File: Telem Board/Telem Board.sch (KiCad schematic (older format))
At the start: 21 parts, among them J1 MAIN, J2 NTC1, J3 NTC2, J4 NTC3, J5 NTC4, J6 6S, U1 LM1117-3.3, U2 MCP3208

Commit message: finish sch
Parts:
- added C8, C9: 1uF, Capacitor_SMD:C_0805_2012Metric_Pad1.18x1.45mm_HandSolder, symbol Device:C
- added H1, H2, H3, H4: MountingHole, MountingHole:MountingHole_3.2mm_M3, symbol Mechanical:MountingHole
- C1, C2, C3, C4, C6, C7: footprint (none) -> Capacitor_SMD:C_0805_2012Metric_Pad1.18x1.45mm_HandSolder
- C5: value 1uF -> 0.47uF; footprint (none) -> Capacitor_SMD:C_0805_2012Metric_Pad1.18x1.45mm_HandSolder
- J1: footprint (none) -> Connector_PinHeader_2.54mm:PinHeader_1x07_P2.54mm_Vertical
- J2, J3, J4, J5: footprint (none) -> Connector_PinHeader_2.54mm:PinHeader_1x02_P2.54mm_Vertical
- J6: footprint (none) -> Connector_AMASS:AMASS_XT60-M_1x02_P7.20mm_Vertical
- R1, R2, R3, R4, R5, R6: footprint (none) -> Capacitor_SMD:C_1206_3216Metric_Pad1.33x1.80mm_HandSolder
- U1: footprint (none) -> Package_TO_SOT_SMD:SOT-223-3_TabPin2
- U2: footprint (none) -> Package_DIP:DIP-16_W7.62mm
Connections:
- net +3V3: now also C8.1, C9.1
- net GNDA: now also C8.2, C9.2
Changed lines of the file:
@@
 F 0 "U2" H 5000 3650 50  0000 C CNN
 F 1 "MCP3208" H 5000 3550 50  0000 C CNN
-F 2 "" H 5450 3150 50  0001 C CNN
+F 2 "Package_DIP:DIP-16_W7.62mm" H 5450 3150 50  0001 C CNN
 F 3 "http://ww1.microchip.com/downloads/en/DeviceDoc/21298c.pdf" H 5450 3150 50  0001 C CNN
 	1    5350 3050
@@
 F 0 "J1" H 7722 3024 50  0000 R CNN
 F 1 "MAIN" H 7722 2933 50  0000 R CNN
-F 2 "" H 7750 3000 50  0001 C CNN
+F 2 "Connector_PinHeader_2.54mm:PinHeader_1x07_P2.54mm_Vertical" H 7750 3000 50  0001 C CNN
 F 3 "~" H 7750 3000 50  0001 C CNN
 	1    7750 3000
@@
 F 0 "U1" H 6750 2342 50  0000 C CNN
 F 1 "LM1117-3.3" H 6750 2251 50  0000 C CNN
-F 2 "" H 6750 2100 50  0001 C CNN
+F 2 "Package_TO_SOT_SMD:SOT-223-3_TabPin2" H 6750 2100 50  0001 C CNN
 F 3 "http://www.ti.com/lit/ds/symlink/lm1117.pdf" H 6750 2100 50  0001 C CNN
 	1    6750 2100
@@
 F 0 "C7" H 7265 2296 50  0000 L CNN
 F 1 "10uF" H 7265 2205 50  0000 L CNN
-F 2 "" H 7188 2100 50  0001 C CNN
+F 2 "Capacitor_SMD:C_0805_2012Metric_Pad1.18x1.45mm_HandSolder" H 7188 2100 50  0001 C CNN
 F 3 "~" H 7150 2250 50  0001 C CNN
 	1    7150 2250
@@
 F 0 "C6" H 6315 2296 50  0000 L CNN
 F 1 "10uF" H 6315 2205 50  0000 L CNN
-F 2 "" H 6238 2100 50  0001 C CNN
+F 2 "Capacitor_SMD:C_0805_2012Metric_Pad1.18x1.45mm_HandSolder" H 6238 2100 50  0001 C CNN
 F 3 "~" H 6200 2250 50  0001 C CNN
 	1    6200 2250
@@
 F 0 "R1" H 3350 2350 50  0000 L CNN
 F 1 "33K" V 3300 2250 50  0000 L CNN
-F 2 "" V 3230 2350 50  0001 C CNN
+F 2 "Capacitor_SMD:C_1206_3216Metric_Pad1.33x1.80mm_HandSolder" V 3230 2350 50  0001 C CNN
 F 3 "~" H 3300 2350 50  0001 C CNN
 	1    3300 2350
@@
 P 3650 1150
 F 0 "R5" H 3720 1196 50  0000 L CNN
-F 1 "250K" H 3720 1105 50  0000 L CNN
-F 2 "" V 3580 1150 50  0001 C CNN
+F 1 "250K" V 3650 1050 50  0000 L CNN
+F 2 "Capacitor_SMD:C_1206_3216Metric_Pad1.33x1.80mm_HandSolder" V 3580 1150 50  0001 C CNN
 F 3 "~" H 3650 1150 50  0001 C CNN
 	1    3650 1150
@@
 P 3650 1550
 F 0 "R6" H 3720 1596 50  0000 L CNN
-F 1 "27K" H 3720 1505 50  0000 L CNN
-F 2 "" V 3580 1550 50  0001 C CNN
+F 1 "27K" V 3650 1450 50  0000 L CNN
+F 2 "Capacitor_SMD:C_1206_3216Metric_Pad1.33x1.80mm_HandSolder" V 3580 1550 50  0001 C CNN
 F 3 "~" H 3650 1550 50  0001 C CNN
 	1    3650 1550
@@
 F 0 "J6" H 2858 1181 50  0000 C CNN
 F 1 "6S" H 2858 1090 50  0000 C CNN
-F 2 "" H 2750 1000 50  0001 C CNN
+F 2 "Connector_AMASS:AMASS_XT60-M_1x02_P7.20mm_Vertical" H 2750 1000 50  0001 C CNN
 F 3 "~" H 2750 1000 50  0001 C CNN
 	1    2750 1000
@@
 P 4050 1500
 F 0 "C5" H 4165 1546 50  0000 L CNN
-F 1 "1uF" H 4165 1455 50  0000 L CNN
-F 2 "" H 4088 1350 50  0001 C CNN
+F 1 "0.47uF" H 4165 1455 50  0000 L CNN
+F 2 "Capacitor_SMD:C_0805_2012Metric_Pad1.18x1.45mm_HandSolder" H 4088 1350 50  0001 C CNN
 F 3 "~" H 4050 1500 50  0001 C CNN
 	1    4050 1500
@@
 F 0 "J2" H 2858 2681 50  0000 C CNN
 F 1 "NTC1" H 2858 2590 50  0000 C CNN
-F 2 "" H 2750 2500 50  0001 C CNN
+F 2 "Connector_PinHeader_2.54mm:PinHeader_1x02_P2.54mm_Vertical" H 2750 2500 50  0001 C CNN
 F 3 "~" H 2750 2500 50  0001 C CNN
 	1    2750 2500
@@
 F 0 "C1" H 3415 2696 50  0000 L CNN
 F 1 "0.1uF" H 3415 2605 50  0000 L CNN
-F 2 "" H 3338 2500 50  0001 C CNN
+F 2 "Capacitor_SMD:C_0805_2012Metric_Pad1.18x1.45mm_HandSolder" H 3338 2500 50  0001 C CNN
 F 3 "~" H 3300 2650 50  0001 C CNN
 	1    3300 2650
@@
 F 0 "R2" H 3350 3000 50  0000 L CNN
 F 1 "33K" V 3300 2900 50  0000 L CNN
-F 2 "" V 3230 3000 50  0001 C CNN
+F 2 "Capacitor_SMD:C_1206_3216Metric_Pad1.33x1.80mm_HandSolder" V 3230 3000 50  0001 C CNN
 F 3 "~" H 3300 3000 50  0001 C CNN
 	1    3300 3000
@@
 F 0 "R3" H 3350 3650 50  0000 L CNN
 F 1 "33K" V 3300 3550 50  0000 L CNN
-F 2 "" V 3230 3650 50  0001 C CNN
+F 2 "Capacitor_SMD:C_1206_3216Metric_Pad1.33x1.80mm_HandSolder" V 3230 3650 50  0001 C CNN
 F 3 "~" H 3300 3650 50  0001 C CNN
 	1    3300 3650
@@
 F 0 "R4" H 3350 4300 50  0000 L CNN
 F 1 "33K" V 3300 4200 50  0000 L CNN
-F 2 "" V 3230 4300 50  0001 C CNN
+F 2 "Capacitor_SMD:C_1206_3216Metric_Pad1.33x1.80mm_HandSolder" V 3230 4300 50  0001 C CNN
 F 3 "~" H 3300 4300 50  0001 C CNN
 	1    3300 4300
@@
 F 0 "C2" H 3415 3346 50  0000 L CNN
 F 1 "0.1uF" H 3415 3255 50  0000 L CNN
-F 2 "" H 3338 3150 50  0001 C CNN
+F 2 "Capacitor_SMD:C_0805_2012Metric_Pad1.18x1.45mm_HandSolder" H 3338 3150 50  0001 C CNN
 F 3 "~" H 3300 3300 50  0001 C CNN
 	1    3300 3300
@@
 F 0 "J5" H 2858 4631 50  0000 C CNN
 F 1 "NTC4" H 2858 4540 50  0000 C CNN
-F 2 "" H 2750 4450 50  0001 C CNN
+F 2 "Connector_PinHeader_2.54mm:PinHeader_1x02_P2.54mm_Vertical" H 2750 4450 50  0001 C CNN
 F 3 "~" H 2750 4450 50  0001 C CNN
 	1    2750 4450
@@
 F 0 "J4" H 2858 3981 50  0000 C CNN
 F 1 "NTC3" H 2858 3890 50  0000 C CNN
-F 2 "" H 2750 3800 50  0001 C CNN
+F 2 "Connector_PinHeader_2.54mm:PinHeader_1x02_P2.54mm_Vertical" H 2750 3800 50  0001 C CNN
 F 3 "~" H 2750 3800 50  0001 C CNN
 	1    2750 3800
@@
 F 0 "J3" H 2858 3331 50  0000 C CNN
 F 1 "NTC2" H 2858 3240 50  0000 C CNN
-F 2 "" H 2750 3150 50  0001 C CNN
+F 2 "Connector_PinHeader_2.54mm:PinHeader_1x02_P2.54mm_Vertical" H 2750 3150 50  0001 C CNN
 F 3 "~" H 2750 3150 50  0001 C CNN
 	1    2750 3150
@@
 F 0 "C3" H 3415 3996 50  0000 L CNN
 F 1 "0.1uF" H 3415 3905 50  0000 L CNN
-F 2 "" H 3338 3800 50  0001 C CNN
+F 2 "Capacitor_SMD:C_0805_2012Metric_Pad1.18x1.45mm_HandSolder" H 3338 3800 50  0001 C CNN
 F 3 "~" H 3300 3950 50  0001 C CNN
 	1    3300 3950
@@
 F 0 "C4" H 3415 4646 50  0000 L CNN
 F 1 "0.1uF" H 3415 4555 50  0000 L CNN
-F 2 "" H 3338 4450 50  0001 C CNN
+F 2 "Capacitor_SMD:C_0805_2012Metric_Pad1.18x1.45mm_HandSolder" H 3338 4450 50  0001 C CNN
 F 3 "~" H 3300 4600 50  0001 C CNN
 	1    3300 4600
@@
 Text Notes 2300 650  0    50   ~ 0
 Input capacitors used to reduce effective input impedance
+$Comp
+L Mechanical:MountingHole H1
+U 1 1 61908367
+P 8600 750
+F 0 "H1" H 8700 796 50  0000 L CNN
+F 1 "MountingHole" H 8700 705 50  0000 L CNN
+F 2 "MountingHole:MountingHole_3.2mm_M3" H 8600 750 50  0001 C CNN
+F 3 "~" H 8600 750 50  0001 C CNN
+	1    8600 750
+	1    0    0    -1
+$EndComp
+$Comp
+L Mechanical:MountingHole H2
+U 1 1 61908C54
+P 9350 750
+F 0 "H2" H 9450 796 50  0000 L CNN
+F 1 "MountingHole" H 9450 705 50  0000 L CNN
+F 2 "MountingHole:MountingHole_3.2mm_M3" H 9350 750 50  0001 C CNN
+F 3 "~" H 9350 750 50  0001 C CNN
+	1    9350 750
+	1    0    0    -1
+$EndComp
+$Comp
+L Mechanical:MountingHole H3
+U 1 1 61909B9E
+P 8600 1000
+F 0 "H3" H 8700 1046 50  0000 L CNN
+F 1 "MountingHole" H 8700 955 50  0000 L CNN
+F 2 "MountingHole:MountingHole_3.2mm_M3" H 8600 1000 50  0001 C CNN
+F 3 "~" H 8600 1000 50  0001 C CNN
+	1    8600 1000
+	1    0    0    -1
+$EndComp
+$Comp
+L Mechanical:MountingHole H4
+U 1 1 6190AC4C
+P 9350 1000
+F 0 "H4" H 9450 1046 50  0000 L CNN
+F 1 "MountingHole" H 9450 955 50  0000 L CNN
+F 2 "MountingHole:MountingHole_3.2mm_M3" H 9350 1000 50  0001 C CNN
+F 3 "~" H 9350 1000 50  0001 C CNN
+	1    9350 1000
+	1    0    0    -1
+$EndComp
+$Comp
+L Device:C C9
+U 1 1 61914F1A
+P 6350 2700
+F 0 "C9" H 6465 2746 50  0000 L CNN
+F 1 "1uF" H 6465 2655 50  0000 L CNN
+F 2 "Capacitor_SMD:C_0805_2012Metric_Pad1.18x1.45mm_HandSolder" H 6388 2550 50  0001 C CNN
+F 3 "~" H 6350 2700 50  0001 C CNN
+	1    6350 2700
+	1    0    0    -1
+$EndComp
+$Comp
+L Device:C C8
+U 1 1 61915AD3
+P 4250 2700
+F 0 "C8" H 4365 2746 50  0000 L CNN
+F 1 "1uF" H 4365 2655 50  0000 L CNN
+F 2 "Capacitor_SMD:C_0805_2012Metric_Pad1.18x1.45mm_HandSolder" H 4288 2550 50  0001 C CNN
+F 3 "~" H 4250 2700 50  0001 C CNN
+	1    4250 2700
+	1    0    0    -1
+$EndComp
+Wire Wire Line
+	5250 2550 4250 2550
+Connection ~ 5250 2550
+Wire Wire Line
+	4250 2850 4250 3650
+Wire Wire Line
+	4250 3650 5250 3650
+Wire Wire Line
+	5550 2550 6350 2550
+Wire Wire Line
+	6350 2850 6350 3650
+Wire Wire Line
+	6350 3650 5550 3650
 $EndSCHEMATC

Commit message: route
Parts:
- removed C9: 1uF, Capacitor_SMD:C_0805_2012Metric_Pad1.18x1.45mm_HandSolder, symbol Device:C
- removed H3, H4: MountingHole, MountingHole:MountingHole_3.2mm_M3, symbol Mechanical:MountingHole
- H1, H2: footprint MountingHole:MountingHole_3.2mm_M3 -> MountingHole:MountingHole_2.7mm_M2.5
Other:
- moved on the sheet: C8
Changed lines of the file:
@@
 	1    0    0    -1
 $EndComp
-Wire Wire Line
-	5550 2550 5250 2550
 Connection ~ 5550 2550
 $Comp
@@
 	1    0    0    -1
 $EndComp
-Wire Wire Line
-	5550 3650 5250 3650
 Connection ~ 5550 3650
 Connection ~ 5250 3650
@@
 F 0 "H1" H 8700 796 50  0000 L CNN
 F 1 "MountingHole" H 8700 705 50  0000 L CNN
-F 2 "MountingHole:MountingHole_3.2mm_M3" H 8600 750 50  0001 C CNN
+F 2 "MountingHole:MountingHole_2.7mm_M2.5" H 8600 750 50  0001 C CNN
 F 3 "~" H 8600 750 50  0001 C CNN
 	1    8600 750
@@
 F 0 "H2" H 9450 796 50  0000 L CNN
 F 1 "MountingHole" H 9450 705 50  0000 L CNN
-F 2 "MountingHole:MountingHole_3.2mm_M3" H 9350 750 50  0001 C CNN
+F 2 "MountingHole:MountingHole_2.7mm_M2.5" H 9350 750 50  0001 C CNN
 F 3 "~" H 9350 750 50  0001 C CNN
 	1    9350 750
@@
 $EndComp
 $Comp
-L Mechanical:MountingHole H3
-U 1 1 61909B9E
-P 8600 1000
-F 0 "H3" H 8700 1046 50  0000 L CNN
-F 1 "MountingHole" H 8700 955 50  0000 L CNN
-F 2 "MountingHole:MountingHole_3.2mm_M3" H 8600 1000 50  0001 C CNN
-F 3 "~" H 8600 1000 50  0001 C CNN
-	1    8600 1000
-	1    0    0    -1
-$EndComp
-$Comp
-L Mechanical:MountingHole H4
-U 1 1 6190AC4C
-P 9350 1000
-F 0 "H4" H 9450 1046 50  0000 L CNN
-F 1 "MountingHole" H 9450 955 50  0000 L CNN
-F 2 "MountingHole:MountingHole_3.2mm_M3" H 9350 1000 50  0001 C CNN
-F 3 "~" H 9350 1000 50  0001 C CNN
-	1    9350 1000
-	1    0    0    -1
-$EndComp
-$Comp
-L Device:C C9
-U 1 1 61914F1A
+L Device:C C8
+U 1 1 61915AD3
 P 6350 2700
-F 0 "C9" H 6465 2746 50  0000 L CNN
+F 0 "C8" H 6465 2746 50  0000 L CNN
 F 1 "1uF" H 6465 2655 50  0000 L CNN
 F 2 "Capacitor_SMD:C_0805_2012Metric_Pad1.18x1.45mm_HandSolder" H 6388 2550 50  0001 C CNN
@@
 	1    0    0    -1
 $EndComp
-$Comp
-L Device:C C8
-U 1 1 61915AD3
-P 4250 2700
-F 0 "C8" H 4365 2746 50  0000 L CNN
-F 1 "1uF" H 4365 2655 50  0000 L CNN
-F 2 "Capacitor_SMD:C_0805_2012Metric_Pad1.18x1.45mm_HandSolder" H 4288 2550 50  0001 C CNN
-F 3 "~" H 4250 2700 50  0001 C CNN
-	1    4250 2700
-	1    0    0    -1
-$EndComp
-Wire Wire Line
-	5250 2550 4250 2550
-Connection ~ 5250 2550
-Wire Wire Line
-	4250 2850 4250 3650
-Wire Wire Line
-	4250 3650 5250 3650
-Wire Wire Line
-	5550 2550 6350 2550
+Wire Wire Line
+	6350 2550 5550 2550
 Wire Wire Line
 	6350 2850 6350 3650
 Wire Wire Line
-	6350 3650 5550 3650
+	5250 2550 5550 2550
+Wire Wire Line
+	5550 3650 6350 3650
+Wire Wire Line
+	5250 3650 5550 3650
 $EndSCHEMATC

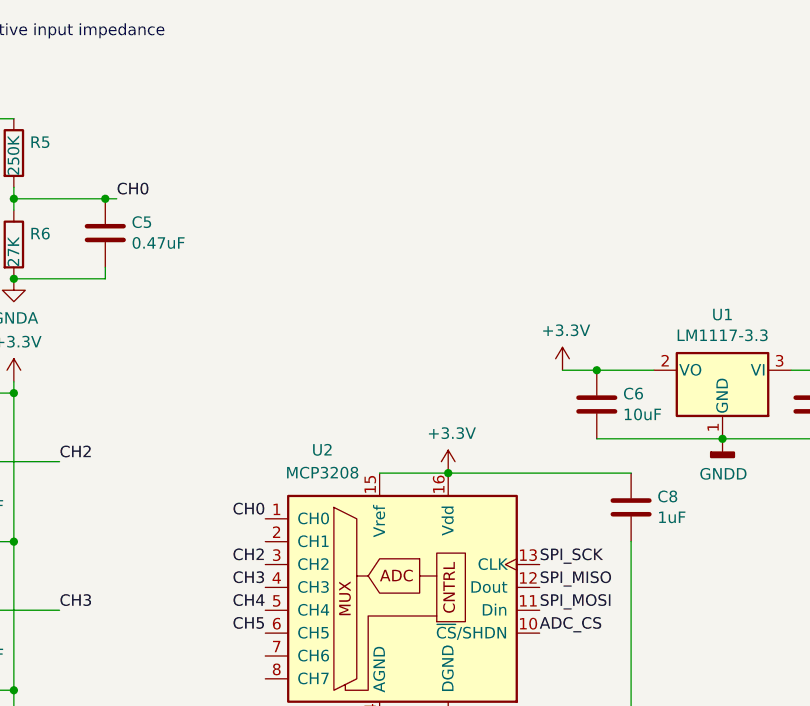
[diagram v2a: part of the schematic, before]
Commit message: add 3s battery in
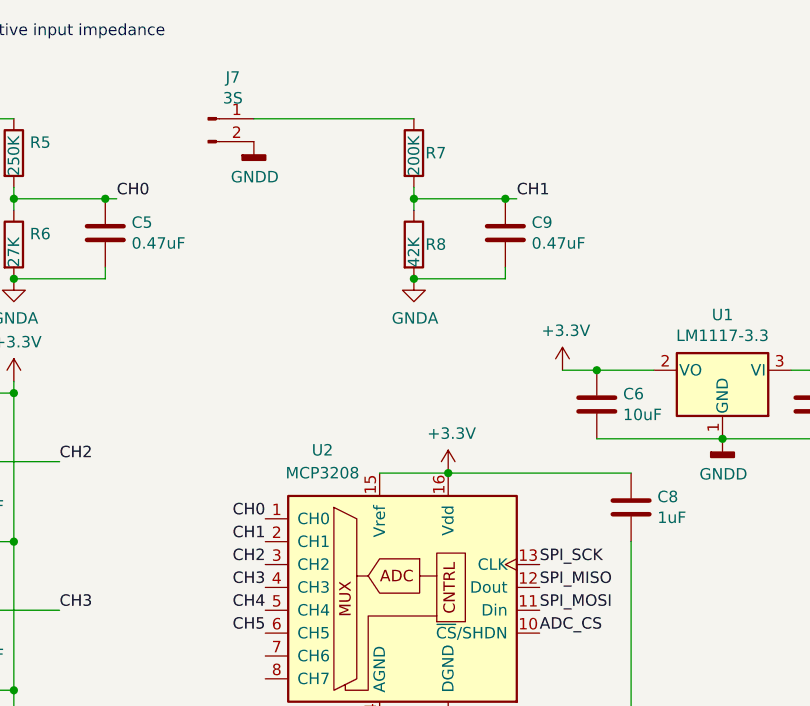
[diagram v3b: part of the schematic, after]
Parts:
- added C9: 0.47uF, Capacitor_SMD:C_0805_2012Metric_Pad1.18x1.45mm_HandSolder, symbol Device:C
- added J7: 3S, Connector_AMASS:AMASS_XT60-M_1x02_P7.20mm_Vertical, symbol Connector:Conn_01x02_Male
- added R7: 200K, Capacitor_SMD:C_1206_3216Metric_Pad1.33x1.80mm_HandSolder, symbol Device:R
- added R8: 42K, Capacitor_SMD:C_1206_3216Metric_Pad1.33x1.80mm_HandSolder, symbol Device:R
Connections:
- net GNDA: now also C9.2, J7.2 (Pin_2), R8.2
- net CH1: now reaches U2.2 (CH1)
- net CH1: now also C9.1, R7.2, R8.1
- new net: J7.1 (Pin_1), R7.1
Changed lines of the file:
@@
 Wire Wire Line
 	5250 3650 5550 3650
+$Comp
+L Device:R R7
+U 1 1 6191565F
+P 5400 1150
+F 0 "R7" H 5450 1150 50  0000 L CNN
+F 1 "200K" V 5400 1050 50  0000 L CNN
+F 2 "Capacitor_SMD:C_1206_3216Metric_Pad1.33x1.80mm_HandSolder" V 5330 1150 50  0001 C CNN
+F 3 "~" H 5400 1150 50  0001 C CNN
+	1    5400 1150
+	1    0    0    -1
+$EndComp
+$Comp
+L Device:R R8
+U 1 1 61915665
+P 5400 1550
+F 0 "R8" H 5450 1550 50  0000 L CNN
+F 1 "42K" V 5400 1450 50  0000 L CNN
+F 2 "Capacitor_SMD:C_1206_3216Metric_Pad1.33x1.80mm_HandSolder" V 5330 1550 50  0001 C CNN
+F 3 "~" H 5400 1550 50  0001 C CNN
+	1    5400 1550
+	1    0    0    -1
+$EndComp
+$Comp
+L power:GNDA #PWR014
+U 1 1 6191566B
+P 5400 1700
+F 0 "#PWR014" H 5400 1450 50  0001 C CNN
+F 1 "GNDA" H 5405 1527 50  0000 C CNN
+F 2 "" H 5400 1700 50  0001 C CNN
+F 3 "" H 5400 1700 50  0001 C CNN
+	1    5400 1700
+	1    0    0    -1
+$EndComp
+Wire Wire Line
+	5400 1300 5400 1350
+Connection ~ 5400 1350
+Wire Wire Line
+	5400 1350 5400 1400
+Text Label 5850 1350 0    50   ~ 0
+CH1
+$Comp
+L Connector:Conn_01x02_Male J7
+U 1 1 61915675
+P 4500 1000
+F 0 "J7" H 4608 1181 50  0000 C CNN
+F 1 "3S" H 4608 1090 50  0000 C CNN
+F 2 "Connector_AMASS:AMASS_XT60-M_1x02_P7.20mm_Vertical" H 4500 1000 50  0001 C CNN
+F 3 "~" H 4500 1000 50  0001 C CNN
+	1    4500 1000
+	1    0    0    -1
+$EndComp
+Wire Wire Line
+	4700 1000 5400 1000
+$Comp
+L power:GNDD #PWR013
+U 1 1 6191567C
+P 4700 1100
+F 0 "#PWR013" H 4700 850 50  0001 C CNN
+F 1 "GNDD" H 4704 945 50  0000 C CNN
+F 2 "" H 4700 1100 50  0001 C CNN
+F 3 "" H 4700 1100 50  0001 C CNN
+	1    4700 1100
+	1    0    0    -1
+$EndComp
+Wire Wire Line
+	5400 1350 5800 1350
+$Comp
+L Device:C C9
+U 1 1 61915683
+P 5800 1500
+F 0 "C9" H 5915 1546 50  0000 L CNN
+F 1 "0.47uF" H 5915 1455 50  0000 L CNN
+F 2 "Capacitor_SMD:C_0805_2012Metric_Pad1.18x1.45mm_HandSolder" H 5838 1350 50  0001 C CNN
+F 3 "~" H 5800 1500 50  0001 C CNN
+	1    5800 1500
+	1    0    0    -1
+$EndComp
+Connection ~ 5800 1350
+Wire Wire Line
+	5800 1350 5850 1350
+Wire Wire Line
+	5400 1700 5800 1700
+Wire Wire Line
+	5800 1700 5800 1650
+Connection ~ 5400 1700
+Text Label 4750 2850 2    50   ~ 0
+CH1
 $EndSCHEMATC

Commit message: gerbers
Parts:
- added F1, F2: 125mA, Resistor_SMD:R_1206_3216Metric_Pad1.30x1.75mm_HandSolder, symbol Device:Fuse
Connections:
- net at R7.1: now also F2.1; no longer J7.1 (Pin_1)
- net at R5.1: now also F1.1; no longer J6.1 (Pin_1)
- new net: F2.2, J7.1 (Pin_1)
- new net: F1.2, J6.1 (Pin_1)
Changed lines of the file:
@@
 	1    0    0    -1
 $EndComp
-Wire Wire Line
-	2950 1000 3650 1000
 $Comp
 L power:GNDD #PWR01
@@
 	1    0    0    -1
 $EndComp
-Wire Wire Line
-	4700 1000 5400 1000
 $Comp
 L power:GNDD #PWR013
@@
 Text Label 4750 2850 2    50   ~ 0
 CH1
+$Comp
+L Device:Fuse F1
+U 1 1 61917A23
+P 3500 1000
+F 0 "F1" V 3303 1000 50  0000 C CNN
+F 1 "125mA" V 3394 1000 50  0000 C CNN
+F 2 "Resistor_SMD:R_1206_3216Metric_Pad1.30x1.75mm_HandSolder" V 3430 1000 50  0001 C CNN
+F 3 "~" H 3500 1000 50  0001 C CNN
+	1    3500 1000
+	0    1    1    0
+$EndComp
+$Comp
+L Device:Fuse F2
+U 1 1 61919427
+P 5250 1000
+F 0 "F2" V 5053 1000 50  0000 C CNN
+F 1 "125mA" V 5144 1000 50  0000 C CNN
+F 2 "Resistor_SMD:R_1206_3216Metric_Pad1.30x1.75mm_HandSolder" V 5180 1000 50  0001 C CNN
+F 3 "~" H 5250 1000 50  0001 C CNN
+	1    5250 1000
+	0    1    1    0
+$EndComp
+Wire Wire Line
+	2950 1000 3350 1000
+Wire Wire Line
+	4700 1000 5100 1000
 $EndSCHEMATC

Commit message: use 12s resistor sizes instead of 6s
#1
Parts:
- J6: value 6S -> 12S
- R5: value 250K -> 470K
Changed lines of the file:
@@
 P 3650 1150
 F 0 "R5" H 3720 1196 50  0000 L CNN
-F 1 "250K" V 3650 1050 50  0000 L CNN
+F 1 "470K" V 3650 1050 50  0000 L CNN
 F 2 "Capacitor_SMD:C_1206_3216Metric_Pad1.33x1.80mm_HandSolder" V 3580 1150 50  0001 C CNN
 F 3 "~" H 3650 1150 50  0001 C CNN
@@
 P 2750 1000
 F 0 "J6" H 2858 1181 50  0000 C CNN
-F 1 "6S" H 2858 1090 50  0000 C CNN
+F 1 "12S" H 2858 1090 50  0000 C CNN
 F 2 "Connector_AMASS:AMASS_XT60-M_1x02_P7.20mm_Vertical" H 2750 1000 50  0001 C CNN
 F 3 "~" H 2750 1000 50  0001 C CNN

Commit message: update values
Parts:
- R6: value 27K -> 22K
- R8: value 42K -> 43K
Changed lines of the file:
@@
 P 3650 1550
 F 0 "R6" H 3720 1596 50  0000 L CNN
-F 1 "27K" V 3650 1450 50  0000 L CNN
+F 1 "22K" V 3650 1450 50  0000 L CNN
 F 2 "Capacitor_SMD:C_1206_3216Metric_Pad1.33x1.80mm_HandSolder" V 3580 1550 50  0001 C CNN
 F 3 "~" H 3650 1550 50  0001 C CNN
@@
 P 5400 1550
 F 0 "R8" H 5450 1550 50  0000 L CNN
-F 1 "42K" V 5400 1450 50  0000 L CNN
+F 1 "43K" V 5400 1450 50  0000 L CNN
 F 2 "Capacitor_SMD:C_1206_3216Metric_Pad1.33x1.80mm_HandSolder" V 5330 1550 50  0001 C CNN
 F 3 "~" H 5400 1550 50  0001 C CNN
